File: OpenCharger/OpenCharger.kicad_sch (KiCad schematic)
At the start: 3 parts, among them J1 Conn_01x02, J2 Conn_01x03, J3 Conn_01x02

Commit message: updated
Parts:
- removed J1: Conn_01x02, Connector:Banana_Jack_2Pin, symbol Connector_Generic:Conn_01x02
- added J1, J6: Conn_01x01_Female, Connector:Banana_Jack_1Pin, symbol Connector:Conn_01x01_Female
- added J5: Conn_01x02, Connector_PinHeader_2.54mm:PinHeader_1x02_P2.54mm_Vertical, symbol Connector_Generic:Conn_01x02
- added R13: .1m, symbol Device:R_US
- J2: footprint Connector:Banana_Jack_3Pin -> Connector_PinHeader_2.54mm:PinHeader_1x03_P2.54mm_Vertical
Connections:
- net L1: now also J1.1 (Pin_1)
- net N: now also J6.1 (Pin_1)
- net V_{DC}: now also R13.2
- new net +12V: J5.2 (Pin_2)
- new net +3V3: J5.1 (Pin_1)
- new net ChargeController/I_{in}Sense: R13.1
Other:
- sheet CAN Transiever ports: added none; removed LED0, LED1
- sheet ChargeController ports: added BOOST/~{BUCK}, I_MAX, I_{in}Sense, RXD, START/~{STOP}, SWITCH, TXD; removed Buck_CTL
- sheet Charger Interface ports: added I_MAX, START/~{STOP}; removed none
- sheet DC-DC Converter ports: added BOOST/~{BUCK}, SWITCH; removed Buck_CTL
- sheet FilteredRectifier ports: added 12V0, 3v3; removed none
- moved on the sheet: J3

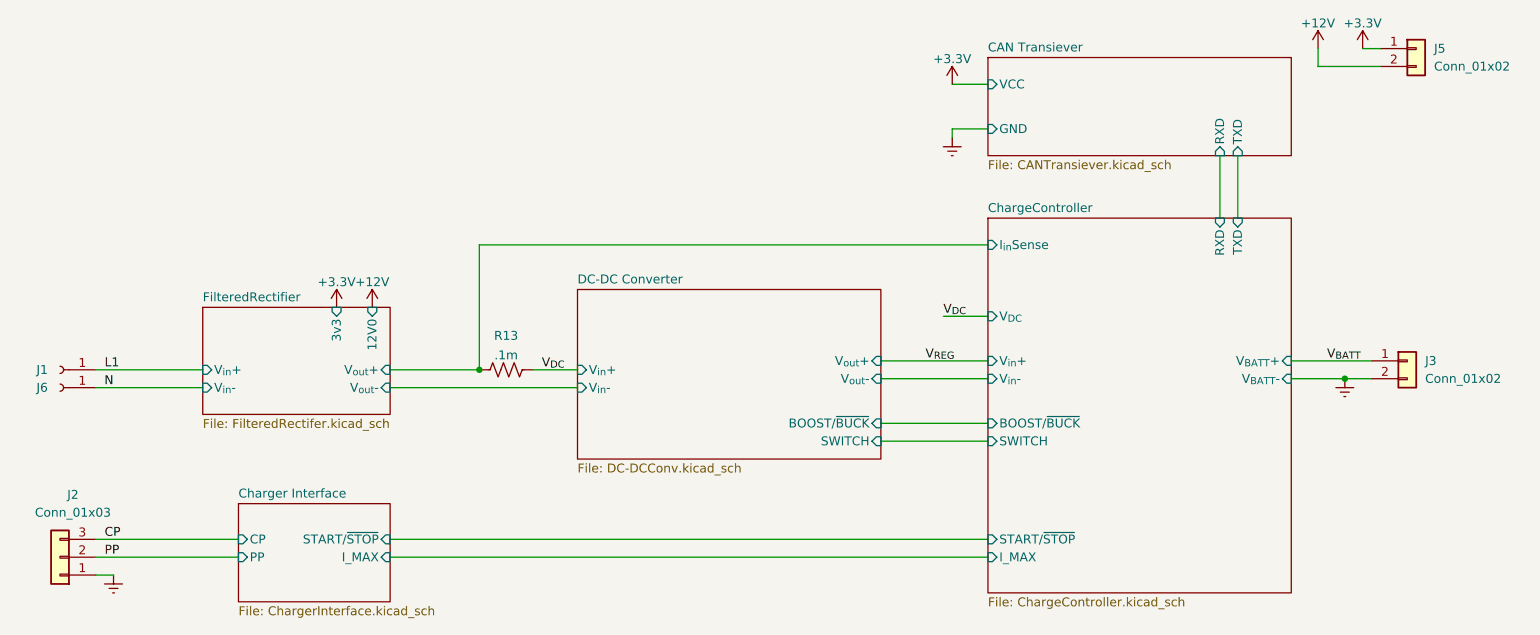
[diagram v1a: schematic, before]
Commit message: Updated Charger and MC
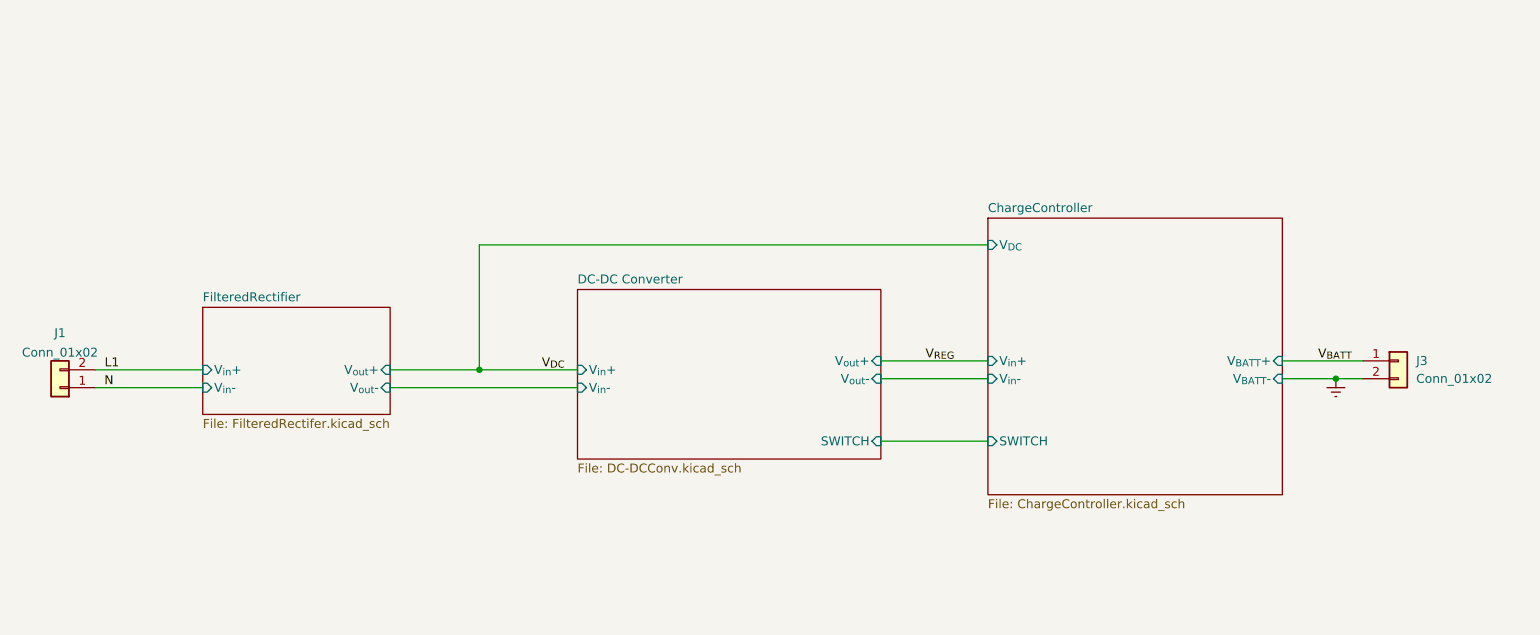
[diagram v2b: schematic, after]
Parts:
- removed J1, J6: Conn_01x01_Female, Connector:Banana_Jack_1Pin, symbol Connector:Conn_01x01_Female
- removed J2: Conn_01x03, Connector_PinHeader_2.54mm:PinHeader_1x03_P2.54mm_Vertical, symbol Connector_Generic:Conn_01x03
- removed J5: Conn_01x02, Connector_PinHeader_2.54mm:PinHeader_1x02_P2.54mm_Vertical, symbol Connector_Generic:Conn_01x02
- removed R13: .1m, symbol Device:R_US
- added J1: Conn_01x02, Connector:Banana_Jack_2Pin, symbol Connector_Generic:Conn_01x02
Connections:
- net L1: now also J1.2 (Pin_2)
- net N: now also J1.1 (Pin_1)
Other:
- removed sheet CAN Transiever
- removed sheet Charger Interface
- sheet ChargeController ports: added none; removed BOOST/~{BUCK}, I_MAX, I_{in}Sense, RXD, START/~{STOP}, TXD
- sheet DC-DC Converter ports: added none; removed BOOST/~{BUCK}
- sheet FilteredRectifier ports: added none; removed 12V0, 3v3
- moved on the sheet: J3
